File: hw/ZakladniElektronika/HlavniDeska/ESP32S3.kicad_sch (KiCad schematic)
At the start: 12 parts, among them J1 ESP-Programing_conector, U10 ESP32-S3-WROOM

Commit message: USB_multiplexer a přehlednost
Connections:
- net IO46-PD is gone; now on net IO03-PD: R6.1, U10.16 (IO46-PD)
- net D+_ESP renamed D+
- net D-_ESP renamed D-
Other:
- moved on the sheet: C132, C133, C134, C135, R10, R6, R7, R8, R9, U10

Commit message: WIP
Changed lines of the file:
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@@
     (effects (font (size 1.27 1.27)) (justify right))
   )
-  (hierarchical_label "5V-(programator)" (shape input) (at 53.34 71.12 90) (fields_autoplaced)
+  (hierarchical_label "5V-(programator)" (shape output) (at 53.34 71.12 90) (fields_autoplaced)
     (effects (font (size 1.27 1.27)) (justify left))
   )

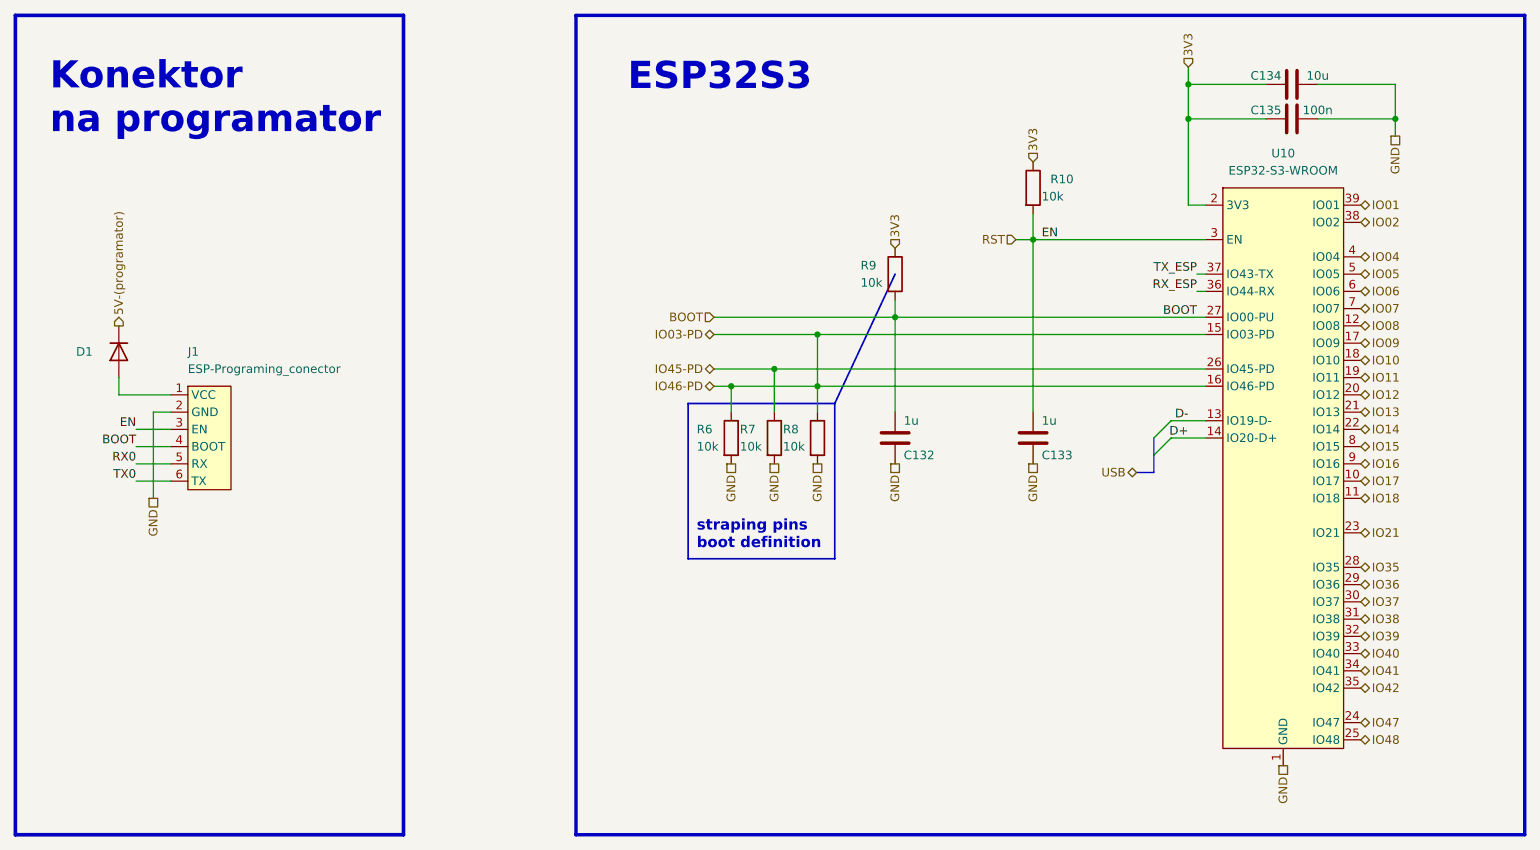
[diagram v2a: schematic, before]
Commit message: Likvidace MiniUI jako samostatné desky a výběr všech komponent
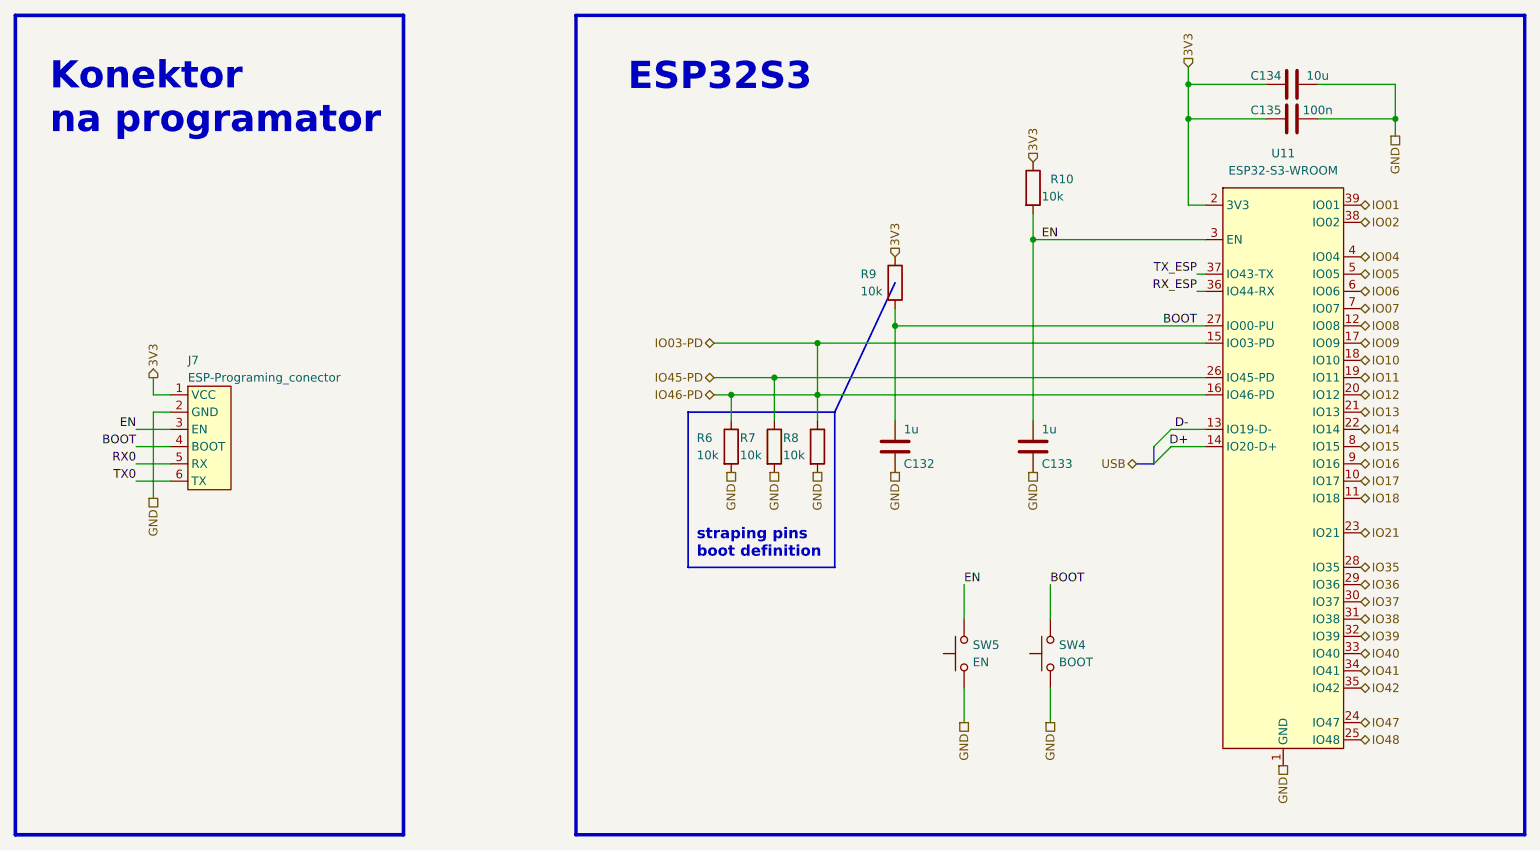
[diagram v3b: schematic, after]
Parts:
- removed D1: ${SIM.PARAMS}, Diode_SMD:D_SMA, symbol Device:D
- removed J1: ESP-Programing_conector, Robotarna_KiCad_Library:ESP-Programing_conector, symbol Robotarna_KiCad_Library:ESP-Programing_conector
- removed U10: ESP32-S3-WROOM, Robotarna_KiCad_Library:ESP32-S3-WROOM, symbol Robotarna_KiCad_Library:ESP32-S3-WROOM
- added J7: ESP-Programing_conector, RKL-ESP:ESP-Programing_conector, symbol RKL-ESP:ESP-Programing_conector
- added SW4: BOOT, RLK-ElectorMechanicalComponents:TCF2QR, symbol Switch:SW_Push
- added SW5: EN, RLK-ElectorMechanicalComponents:TCF2QR, symbol Switch:SW_Push
- added U11: ESP32-S3-WROOM, RKL-ESP:ESP32-S3-WROOM, symbol RKL-ESP:ESP32-S3-WROOM
- C132, C133: info 50V, X7R -> 50V, X5R (potenciálně C52923 což je 25V, X5R )
- C134: Basic/Extended (none) -> B; JLCPCB_CORRECTION 0;0;0 -> (none); info (none) -> 25V, X5R
- R10, R6, R7, R8, R9: Basic/Extended (none) -> B
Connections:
- net 3V3: now also J7.1 (VCC), U11.2 (3V3)
- net BOOT: now also J7.4 (BOOT), SW4.2, U11.27 (IO00-PU)
- net D+: now also U11.14 (IO20-D+)
- net D-: now also U11.13 (IO19-D-)
- net GND: now also J7.2 (GND), SW4.1, SW5.1, U11.1 (GND), U11.40 (GND), U11.41 (GND)
- net IO01: now also U11.39 (IO01)
- net IO02: now also U11.38 (IO02)
- net IO03-PD: now also U11.15 (IO03-PD), U11.16 (IO46-PD)
- net IO04: now also U11.4 (IO04)
- net IO05: now also U11.5 (IO05)
- net IO06: now also U11.6 (IO06)
- net IO07: now also U11.7 (IO07)
- net IO08: now also U11.12 (IO08)
- net IO09: now also U11.17 (IO09)
- net IO10: now also U11.18 (IO10)
- net IO11: now also U11.19 (IO11)
- net IO12: now also U11.20 (IO12)
- net IO13: now also U11.21 (IO13)
- net IO14: now also U11.22 (IO14)
- net IO15: now also U11.8 (IO15)
- net IO16: now also U11.9 (IO16)
- net IO17: now also U11.10 (IO17)
- net IO18: now also U11.11 (IO18)
- net IO21: now also U11.23 (IO21)
- net IO35: now also U11.28 (IO35)
- net IO36: now also U11.29 (IO36)
- net IO37: now also U11.30 (IO37)
- net IO38: now also U11.31 (IO38)
- net IO39: now also U11.32 (IO39)
- net IO40: now also U11.33 (IO40)
- net IO41: now also U11.34 (IO41)
- net IO42: now also U11.35 (IO42)
- net IO45-PD: now also U11.26 (IO45-PD)
- net IO47: now also U11.24 (IO47)
- net IO48: now also U11.25 (IO48)
- net RX0: now also J7.5 (RX)
- net RX_ESP: now also U11.36 (IO44-RX)
- net TX0: now also J7.6 (TX)
- net TX_ESP: now also U11.37 (IO43-TX)
- net RST renamed EN
- net EN: now also J7.3 (EN), SW5.2, U11.3 (EN)
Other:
- moved on the sheet: C132, C133, R6, R7, R8, R9

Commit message: Výmněna ochrany baterie
Předchozí ochranný čip JLCPCB nemělo na skladě
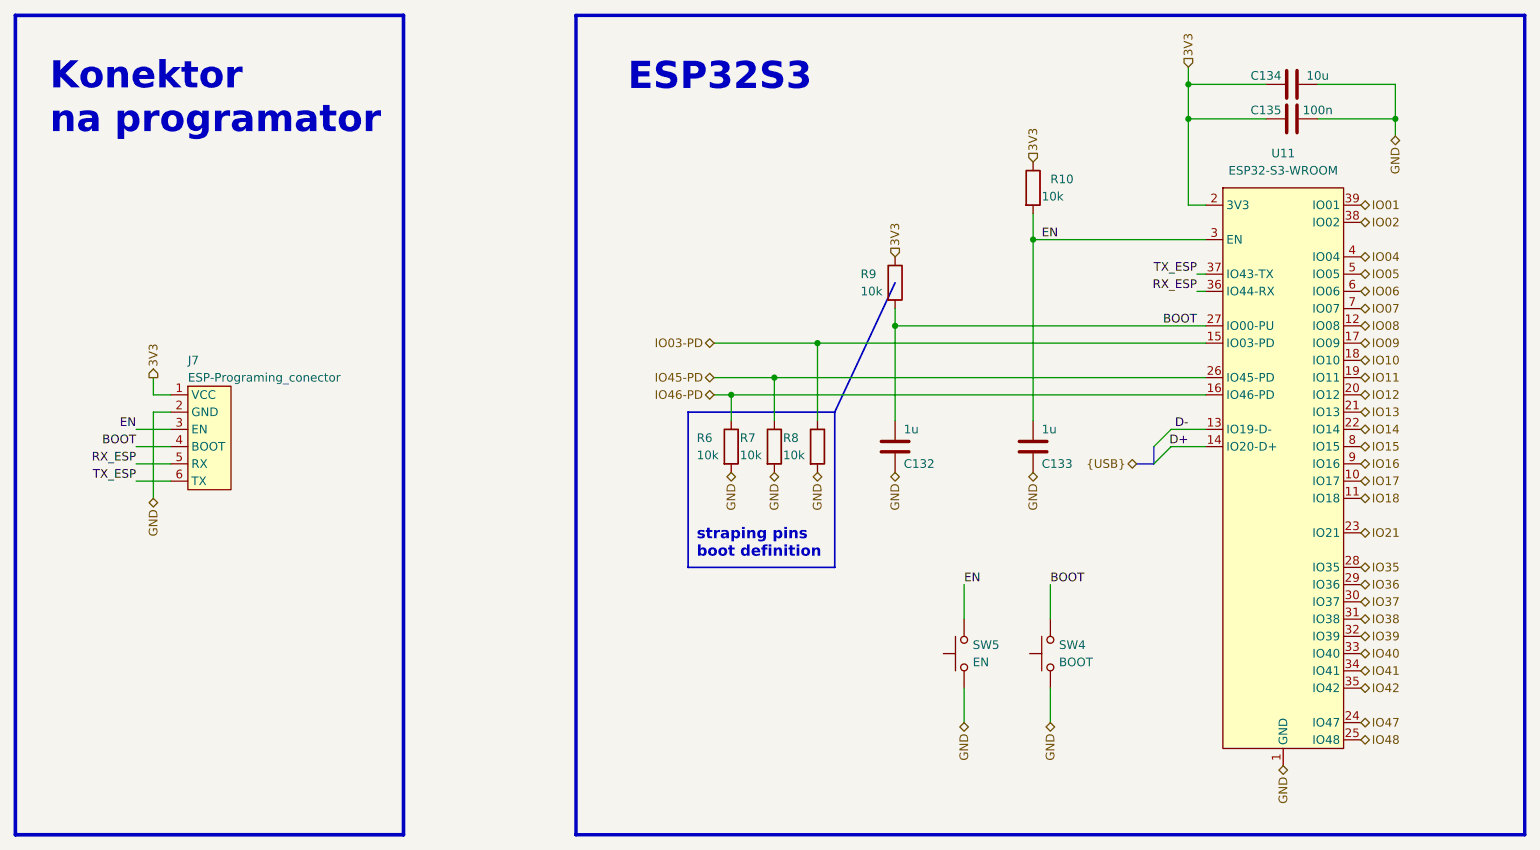
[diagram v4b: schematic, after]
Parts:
- U11: LCSC C2913202 -> C3013946
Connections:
- net RX0 is gone; now on net RX_ESP: J7.5 (RX)
- net TX0 is gone; now on net TX_ESP: J7.6 (TX)
- net IO03-PD: no longer R6.1, U11.16 (IO46-PD)
- new net IO46-PD: R6.1, U11.16 (IO46-PD)
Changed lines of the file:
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@@
   (junction (at 241.3 40.64) (diameter 0) (color 0 0 0 0)
-  )
-  (junction (at 156.21 81.28) (diameter 0) (color 0 0 0 0)
   )
   (junction (at 156.21 73.66) (diameter 0) (color 0 0 0 0)
@@
     (stroke (width 0.5) (type default))
   )
-  (wire (pts (xy 156.21 81.28) (xy 213.36 81.28))
+  (wire (pts (xy 143.51 81.28) (xy 213.36 81.28))
     (stroke (width 0) (type default))
   )
@@
     (stroke (width 0.5) (type default))
   )
-  (wire (pts (xy 143.51 81.28) (xy 156.21 81.28))
-    (stroke (width 0) (type default))
-  )
   (wire (pts (xy 222.25 40.64) (xy 210.82 40.64))
     (stroke (width 0) (type default))
@@
     (stroke (width 0.5) (type default))
   )
-  (wire (pts (xy 156.21 81.28) (xy 156.21 85.09))
+  (wire (pts (xy 156.21 73.66) (xy 156.21 85.09))
     (stroke (width 0) (type default))
   )
@@
     (stroke (width 0.53) (type default))
   )
-  (wire (pts (xy 156.21 73.66) (xy 156.21 81.28))
-    (stroke (width 0) (type default))
-  )
   (wire (pts (xy 190.5 124.46) (xy 190.5 129.54))
     (stroke (width 0) (type default))
@@
     (effects (font (size 1.27 1.27)) (justify right bottom))
   )
-  (label "RX0" (at 55.88 91.44 180) (fields_autoplaced)
+  (label "TX_ESP" (at 55.88 93.98 180) (fields_autoplaced)
     (effects (font (size 1.27 1.27)) (justify right bottom))
   )
   (label "D-" (at 210.82 86.36 180) (fields_autoplaced)
+    (effects (font (size 1.27 1.27)) (justify right bottom))
+  )
+  (label "RX_ESP" (at 55.88 91.44 180) (fields_autoplaced)
     (effects (font (size 1.27 1.27)) (justify right bottom))
   )
@@
     (effects (font (size 1.27 1.27)) (justify left bottom))
   )
-  (label "TX0" (at 55.88 93.98 180) (fields_autoplaced)
-    (effects (font (size 1.27 1.27)) (justify right bottom))
-  )
   (label "D+" (at 210.82 88.9 180) (fields_autoplaced)
     (effects (font (size 1.27 1.27)) (justify right bottom))
@@
     (effects (font (size 1.27 1.27)) (justify left bottom))
   )
-  (hierarchical_label "GND" (shape passive) (at 224.79 135.89 270) (fields_autoplaced)
+  (hierarchical_label "GND" (shape bidirectional) (at 224.79 135.89 270) (fields_autoplaced)
     (effects (font (size 1.27 1.27)) (justify right))
   )
@@
     (effects (font (size 1.27 1.27)) (justify right))
   )
-  (hierarchical_label "GND" (shape passive) (at 143.51 92.71 270) (fields_autoplaced)
+  (hierarchical_label "GND" (shape bidirectional) (at 143.51 92.71 270) (fields_autoplaced)
     (effects (font (size 1.27 1.27)) (justify right))
   )
@@
     (effects (font (size 1.27 1.27)) (justify left))
   )
-  (hierarchical_label "GND" (shape passive) (at 177.8 129.54 270) (fields_autoplaced)
-    (effects (font (size 1.27 1.27)) (justify right))
-  )
-  (hierarchical_label "GND" (shape passive) (at 167.64 92.71 270) (fields_autoplaced)
+  (hierarchical_label "GND" (shape bidirectional) (at 177.8 129.54 270) (fields_autoplaced)
+    (effects (font (size 1.27 1.27)) (justify right))
+  )
+  (hierarchical_label "GND" (shape bidirectional) (at 167.64 92.71 270) (fields_autoplaced)
     (effects (font (size 1.27 1.27)) (justify right))
   )
@@
     (effects (font (size 1.27 1.27)) (justify left))
   )
-  (hierarchical_label "GND" (shape passive) (at 190.5 129.54 270) (fields_autoplaced)
+  (hierarchical_label "GND" (shape bidirectional) (at 190.5 129.54 270) (fields_autoplaced)
     (effects (font (size 1.27 1.27)) (justify right))
   )
@@
     (effects (font (size 1.27 1.27)) (justify left))
   )
-  (hierarchical_label "GND" (shape passive) (at 187.96 92.71 270) (fields_autoplaced)
+  (hierarchical_label "GND" (shape bidirectional) (at 187.96 92.71 270) (fields_autoplaced)
     (effects (font (size 1.27 1.27)) (justify right))
   )
@@
     (effects (font (size 1.27 1.27)) (justify left))
   )
-  (hierarchical_label "GND" (shape passive) (at 156.21 92.71 270) (fields_autoplaced)
-    (effects (font (size 1.27 1.27)) (justify right))
-  )
-  (hierarchical_label "GND" (shape passive) (at 241.3 43.18 270) (fields_autoplaced)
+  (hierarchical_label "GND" (shape bidirectional) (at 156.21 92.71 270) (fields_autoplaced)
+    (effects (font (size 1.27 1.27)) (justify right))
+  )
+  (hierarchical_label "GND" (shape bidirectional) (at 241.3 43.18 270) (fields_autoplaced)
     (effects (font (size 1.27 1.27)) (justify right))
   )
@@
     (effects (font (size 1.27 1.27)) (justify left))
   )
-  (hierarchical_label "USB" (shape bidirectional) (at 203.2 91.44 180) (fields_autoplaced)
+  (hierarchical_label "{USB}" (shape bidirectional) (at 203.2 91.44 180) (fields_autoplaced)
     (effects (font (size 1.27 1.27)) (justify right))
   )
@@
     (effects (font (size 1.27 1.27)) (justify left))
   )
-  (hierarchical_label "GND" (shape passive) (at 149.86 92.71 270) (fields_autoplaced)
+  (hierarchical_label "GND" (shape bidirectional) (at 149.86 92.71 270) (fields_autoplaced)
     (effects (font (size 1.27 1.27)) (justify right))
   )
@@
     (effects (font (size 1.27 1.27)) (justify left))
   )
-  (hierarchical_label "GND" (shape passive) (at 58.42 96.52 270) (fields_autoplaced)
+  (hierarchical_label "GND" (shape bidirectional) (at 58.42 96.52 270) (fields_autoplaced)
     (effects (font (size 1.27 1.27)) (justify right))
   )
@@
       (effects (font (size 1.27 1.27)) hide)
     )
-    (property "LCSC" "C2913202" (at 224.79 38.1 0)
+    (property "LCSC" "C3013946" (at 224.79 38.1 0)
       (effects (font (size 1.27 1.27)) hide)
     )
@@
       (effects (font (size 1.27 1.27)) hide)
     )
-    (property "info" "ESP32-S3-WROOM-1-N16R8" (at 224.79 50.8 0)
+    (property "info" "ESP32-S3-WROOM-1-N16R8" (at 224.79 31.75 0)
       (effects (font (size 1.27 1.27)) hide)
     )
@@
       (effects (font (size 1.27 1.27)) hide)
     )
-    (property "JLCPCB_IGNORE" "ignore" (at 66.04 81.28 0)
-      (effects (font (size 1.27 1.27)) hide)
-    )
+    (property "JLCPCB_IGNORE" "ignore" (at 66.04 64.77 0)
+      (effects (font (size 1.27 1.27)) hide)
+    )

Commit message: AHS-V1
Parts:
- U11: JLCPCB_CORRECTION (none) -> 0;8.89;0; LCSC C3013946 -> C2913202
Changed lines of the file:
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@@
       (effects (font (size 1.27 1.27)) hide)
     )
-    (property "LCSC" "C3013946" (at 224.79 38.1 0)
+    (property "LCSC" "C2913202" (at 224.79 38.1 0)
       (effects (font (size 1.27 1.27)) hide)
     )
@@
       (effects (font (size 1.27 1.27)) hide)
     )
+    (property "JLCPCB_CORRECTION" "0;8.89;0" (at 224.79 50.8 0)
+      (effects (font (size 1.27 1.27)) hide)
+    )

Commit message: Bordel Hw
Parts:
- SW4, SW5: LCSC C240292 -> C495937
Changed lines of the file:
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@@
 			)
 		)
-		(property "LCSC" "C240292"
+		(property "LCSC" "C495937"
 			(at 177.8 119.38 0)
 			(effects
@@
 			)
 		)
-		(property "LCSC" "C240292"
+		(property "LCSC" "C495937"
 			(at 190.5 119.38 0)
 			(effects
